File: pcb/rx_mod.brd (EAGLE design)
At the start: 42 x 28.7 mm, 25 parts, among them U1 ATMEGA328

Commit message: diversity ready version - TESTED
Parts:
- removed 3157: TS5A3157, pimoroni:SOT23-6
- removed ICSP1: 3x2 M, SmartPrj:2X03
- removed OLED: (no value), pinhead:1X04
- removed R_LED: 330, rcl:R0603
- removed R_PD_SWITCH: 10K, rcl:R0805
- removed STATUS: (no value), led:SML0603
- added C3: (no value), adafruit:C0603
- added JP3: (no value), SparkFun-Connectors:1X07
- added JP4: (no value), SparkFun-Connectors:1X04
- added LED_1, LED_2: (no value), led:SML0603
- added R_LED1, R_LED2: 330, rcl:R0603
- added R_RSSI1: 100K, SparkFun:0603-RES
- added U2: (no value), ts5a3359:VFSOP-8
- moved JP2 35.7 mm to (2.58, 8.29), turned to 270 degrees
- moved C_DTR 15.2 mm to (5.35, 14.9), flipped to the bottom
- moved R_PU_RST 15.0 mm to (5.35, 11.2), flipped to the bottom, turned to 270 degrees
- moved R_RSSI 5.95 mm to (27.4, 17.8), turned to 90 degrees
- moved R_CLK 4.89 mm to (36.8, 20.3), turned to 90 degrees
- moved R_VIDEO 4.26 mm to (13.7, 5.74)
- moved R_SYNC 3.56 mm to (16.9, 5.73)
- moved R_SPIDATA 3.28 mm to (33.8, 20.2), turned to 90 degrees
- moved R_VIDOUT 3.11 mm to (20.2, 6.07), turned to 90 degrees
- moved R_SPI_SEL 2.45 mm to (30.1, 20.3), turned to 90 degrees
- moved RECEIVER_A 2.30 mm to (7.07, 25.1)
- moved C2 2.13 mm to (25.3, 6.35)
- moved C1 1.76 mm to (33.3, 6.39)
- moved C_AREF 1.72 mm to (27.5, 14.1)
- moved XTAL1 1.44 mm to (11.2, 12.9)
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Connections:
- net SPI_SEL renamed SPI_SEL_A
- removed net LED_PIN: STATUS.A, U1.22
- new net N$11: LED_2.C, R_LED2.1
- new net RSSI_B: JP3.5, R_RSSI1.2, U1.24
- new net RXVIDOUT2: JP3.4, U2.1
- new net SPI_SEL_B: JP3.2, U1.12
- new net SW_CTRL2: LED_2.A, U1.10, U2.5
- net 5V: now also C3.1, JP3.7, U2.8; no longer 3157.5, ICSP1.2, OLED.4
- net GND: now also C3.2, JP3.6, R_LED1.2, R_LED2.2, R_RSSI1.1, U2.4; no longer 3157.2, ICSP1.6, OLED.3, R_LED.2, R_PD_SWITCH.1
- net MISO: now also JP4.3; no longer ICSP1.1
- net MOSI: now also JP4.2; no longer ICSP1.4
- net N$3: now also LED_1.C, R_LED1.1; no longer R_LED.1, STATUS.C
- net N$6: now also U2.7; no longer RECEIVER_A.VIDEO
- net OSD_VOUT: now also U2.3; no longer 3157.1
- net RESET: now also JP4.1; no longer ICSP1.5
- net RXVIDOUT: now also RECEIVER_A.VIDEO, U2.2; no longer 3157.3, C2.C, R_VIDOUT.2
- net SCK: now also JP4.4; no longer ICSP1.3
- net SCL: no longer OLED.2
- net SDA: no longer OLED.1
- net SPI_CLK: now also JP3.3
- net SPI_DATA: now also JP3.1
- net SW_CTRL: now also LED_1.A, U2.6; no longer 3157.6, R_PD_SWITCH.2
- net VIDOUT: now also C2.C, R_VIDOUT.2; no longer 3157.4
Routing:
- net GND: track 191.1 -> 117.2 mm, vias 4 -> 5
- net 5V: track 140.6 -> 82.7 mm, vias 3 -> 2
- net CH1: track 82.0 -> 45.6 mm, vias 10 -> 2
- net SW_CTRL2: track 0.00 -> 35.9 mm, vias 0 -> 2
- net RXVIDOUT2: track 0.00 -> 33.7 mm, vias 0 -> 1
- net LED_PIN: track 33.6 -> 0.00 mm, vias 4 -> 0
- net SPI_CLK: track 3.74 -> 33.5 mm
- net RXVIDOUT: track 11.7 -> 32.4 mm, vias 0 -> 1
- net SPI_SEL_B: track 0.00 -> 19.0 mm, vias 0 -> 3
- net SW_CTRL: track 20.8 -> 38.9 mm, vias 3 -> 2
- net MOSI: track 44.9 -> 27.8 mm, vias 6 -> 0
- net RSSI_B: track 0.00 -> 15.3 mm, vias 0 -> 1
- net SCK: track 36.8 -> 25.9 mm
- net SCL: track 10.8 -> 0.00 mm, vias 1 -> 0
- net N$6: track 20.6 -> 29.3 mm, vias 3 -> 2
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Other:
- board size 42 x 28.7 mm -> 42 x 28.8 mm
- board text added: "A"
- board text added: "B"
- board text added: "MISO"
- board text added: "MOSI"
- board text added: "OSD"
- board text added: "RST"
- board text added: "RX_VCC"
- board text added: "SCK"
- board text added: "SPI_CLK"
- board text added: "SPI_DATA"
- board text added: "SPI_SEL"
- board text added: "vidout"

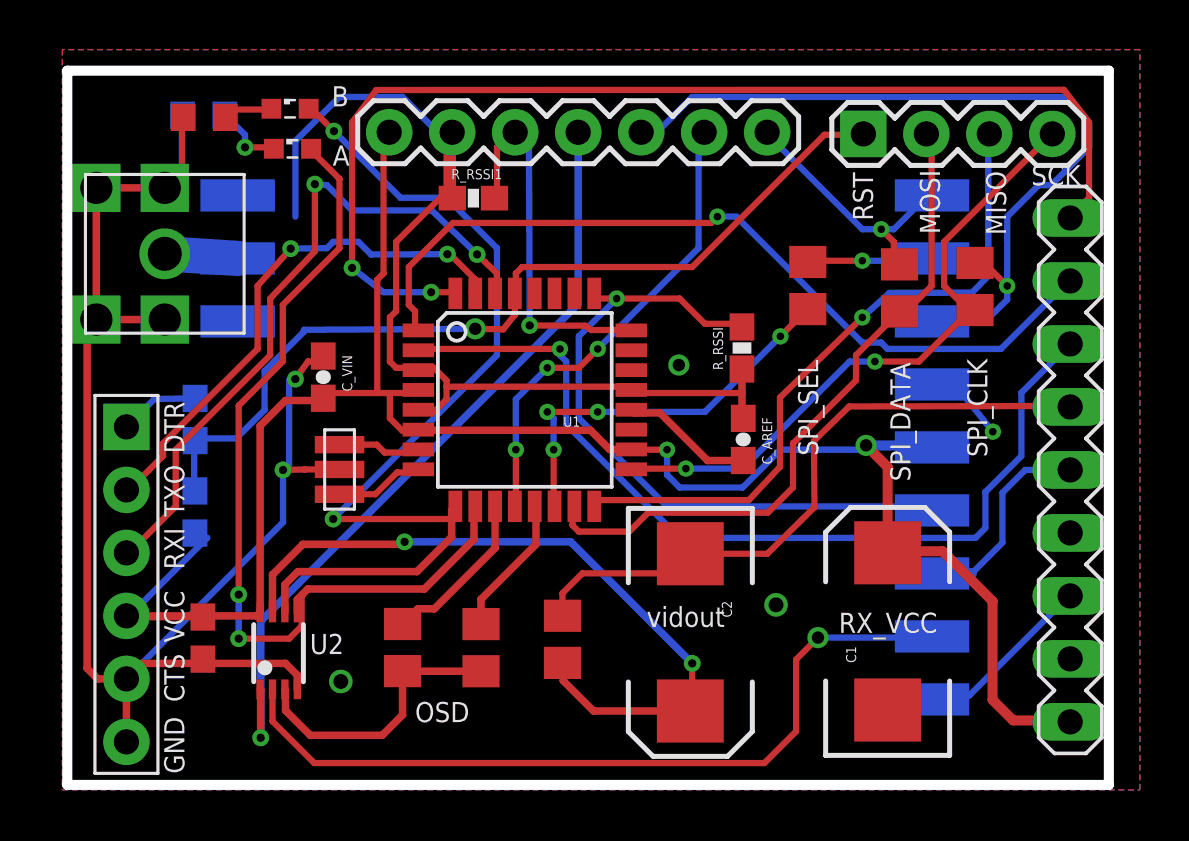
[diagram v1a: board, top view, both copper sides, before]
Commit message: new SMA connetor
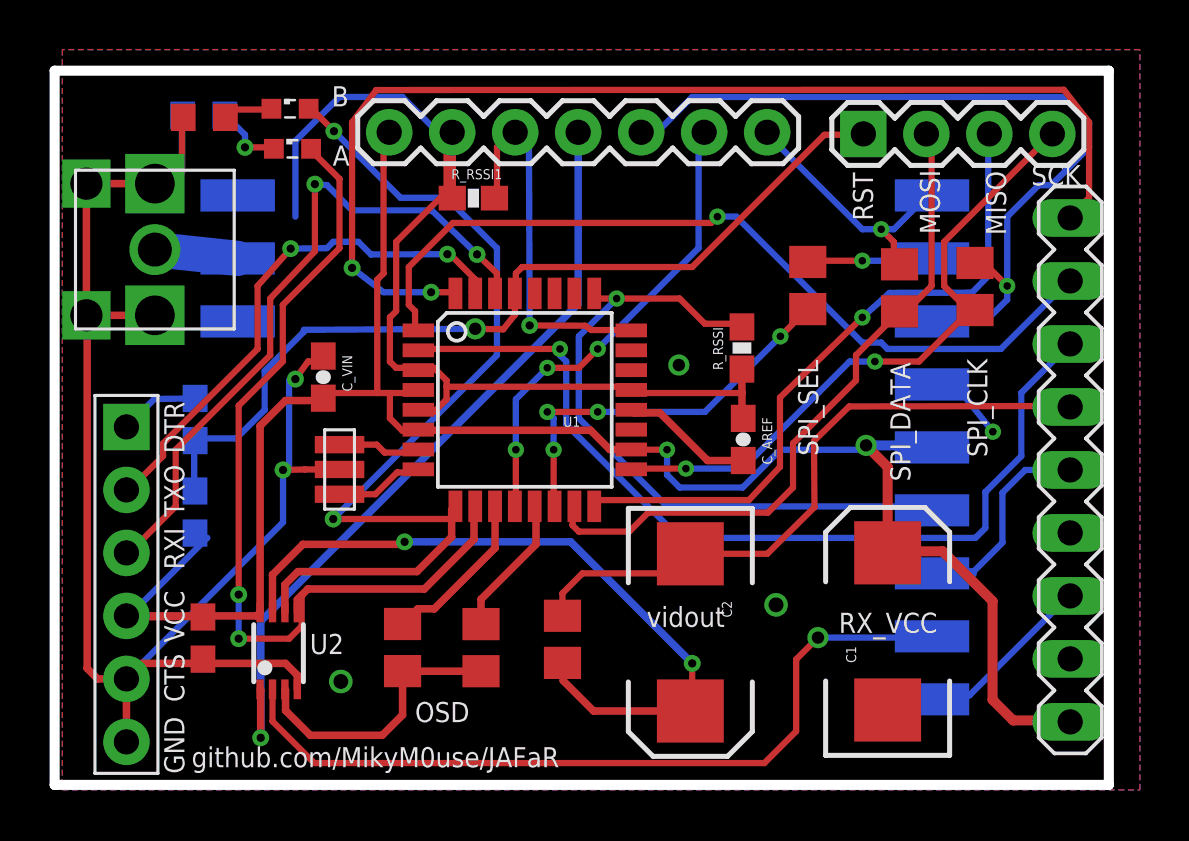
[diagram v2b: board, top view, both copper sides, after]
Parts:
- C1, C2: value (none) -> 470uf
- C3: value (none) -> 0.1uf
- moved U$1 0.43 mm to (3.71, 21.8)
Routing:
- net GND: track 117.2 -> 118.3 mm
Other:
- board size 42 x 28.8 mm -> 42.5 x 28.8 mm
- board text added: "github.com/MikyM0use/JAFaR"
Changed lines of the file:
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@@
 <?xml version="1.0" encoding="utf-8"?>
 <!DOCTYPE eagle SYSTEM "eagle.dtd">
-<eagle version="7.4.0">
+<eagle version="7.5.0">
 <drawing>
 <settings>
@@
 <board>
 <plain>
-<wire x1="0.2" y1="0.2" x2="0.2" y2="29" width="0.4064" layer="20"/>
-<wire x1="0.2" y1="29" x2="42.2" y2="29" width="0.4064" layer="20"/>
+<wire x1="-0.31" y1="0.2" x2="-0.31" y2="29" width="0.4064" layer="20"/>
+<wire x1="-0.31" y1="29" x2="42.2" y2="29" width="0.4064" layer="20"/>
 <wire x1="42.2" y1="29" x2="42.2" y2="0.2" width="0.4064" layer="20"/>
-<wire x1="42.2" y1="0.2" x2="0.2" y2="0.2" width="0.4064" layer="20"/>
+<wire x1="42.2" y1="0.2" x2="-0.31" y2="0.2" width="0.4064" layer="20"/>
 <text x="30.48" y="13.47" size="0.8128" layer="25" rot="R90">SPI_SEL</text>
 <text x="34.2" y="12.44" size="0.8128" layer="25" font="vector" rot="R90">SPI_DATA</text>
@@
 <text x="23.56" y="6.57" size="0.8128" layer="25" font="vector" ratio="9">vidout</text>
 <text x="31.31" y="6.33" size="0.8128" layer="25" font="vector" ratio="9">RX_VCC</text>
+<text x="5.21" y="0.91" size="0.8128" layer="25" font="vector">github.com/MikyM0use/JAFaR</text>
 </plain>
 <attributes>
@@
 </element>
 <element name="XTAL1" library="CSTCE16M0V53-R0" package="CSTCE16M0V53-R0" value="CSTCE16M0V53-R0" x="11.1798" y="12.9198" smashed="yes" rot="R270"/>
-<element name="U$1" library="#fpv" package="SMA_CONNECTOR" value="SMA_ANTENNA" x="4.1146" y="21.6352" rot="R90"/>
-<element name="C1" library="SparkFun-Passives" package="EIA7343" value="" x="33.28" y="6.39" rot="R90"/>
-<element name="C2" library="SparkFun-Passives" package="EIA7343" value="" x="25.3238" y="6.35" rot="R270"/>
+<element name="U$1" library="#fpv" package="SMA_CONNECTOR" value="SMA_ANTENNA" x="3.7146" y="21.8052" rot="R90"/>
+<element name="C1" library="SparkFun-Passives" package="EIA7343" value="470uf" x="33.28" y="6.39" rot="R90"/>
+<element name="C2" library="SparkFun-Passives" package="EIA7343" value="470uf" x="25.3238" y="6.35" rot="R270"/>
 <element name="R_VIDOUT" library="rcl" package="R0805" value="10" x="20.1676" y="6.0706" smashed="yes" rot="R90">
 <attribute name="VALUE" x="20.8562" y="9.0292" size="0.8128" layer="27" font="vector" rot="R180"/>
@@
 <attribute name="VALUE" x="8.28" y="23.85" size="1.27" layer="27"/>
 </element>
-<element name="C3" library="adafruit" package="C0603" value="" x="5.67" y="6.12" smashed="yes" rot="R270">
+<element name="C3" library="adafruit" package="C0603" value="0.1uf" x="5.67" y="6.12" smashed="yes" rot="R270">
 <attribute name="VALUE" x="3.638" y="7.009" size="1.27" layer="27" rot="R270"/>
 </element>
@@
 <wire x1="1.425" y1="4.475" x2="1" y2="4.9" width="0.3048" layer="1"/>
 <wire x1="1" y1="4.9" x2="1" y2="18.5936" width="0.3048" layer="1"/>
-<wire x1="1" y1="18.5936" x2="1.3716" y2="18.9652" width="0.3048" layer="1"/>
-<wire x1="1.3716" y1="18.9652" x2="4.1316" y2="18.9652" width="0.3048" layer="1"/>
-<wire x1="1.3716" y1="24.2752" x2="1.3716" y2="18.9652" width="0.3048" layer="1"/>
-<wire x1="1.3716" y1="24.2752" x2="4.1316" y2="24.2752" width="0.3048" layer="1"/>
+<wire x1="1" y1="18.5936" x2="0.9716" y2="19.1352" width="0.3048" layer="1"/>
+<wire x1="0.9716" y1="19.1352" x2="3.7316" y2="19.1352" width="0.3048" layer="1"/>
+<wire x1="0.9716" y1="24.4452" x2="0.9716" y2="19.1352" width="0.3048" layer="1"/>
+<wire x1="0.9716" y1="24.4452" x2="3.7316" y2="24.4452" width="0.3048" layer="1"/>
 <wire x1="9.475" y1="4.055" x2="9.475" y2="4.625" width="0.3048" layer="1"/>
 <wire x1="9.475" y1="4.625" x2="9" y2="5.1" width="0.3048" layer="1"/>
@@
 <wire x1="4.318" y1="24.384" x2="4.826" y2="24.892" width="0.254" layer="16"/>
 <wire x1="4.826" y1="27.178" x2="4.85" y2="27.2" width="0.254" layer="16"/>
-<wire x1="4.318" y1="24.384" x2="4.1316" y2="24.2752" width="0.254" layer="16"/>
+<wire x1="4.318" y1="24.384" x2="3.7316" y2="24.4452" width="0.254" layer="16"/>
 <wire x1="4.826" y1="24.892" x2="4.826" y2="26.924" width="0.254" layer="1"/>
 <wire x1="4.318" y1="24.384" x2="4.826" y2="24.892" width="0.254" layer="1"/>
 <wire x1="4.826" y1="26.924" x2="4.8746" y2="27.1168" width="0.254" layer="1"/>
-<wire x1="4.318" y1="24.384" x2="4.1316" y2="24.2752" width="0.254" layer="1"/>
+<wire x1="4.318" y1="24.384" x2="3.7316" y2="24.4452" width="0.254" layer="1"/>
 <wire x1="9.906" y1="17.272" x2="10.414" y2="17.272" width="0.254" layer="1"/>
 <wire x1="9.398" y1="16.564" x2="9.906" y2="17.272" width="0.254" layer="1"/>
@@
 <wire x1="9.398" y1="16.564" x2="9.144" y2="16.51" width="0.254" layer="16"/>
 <wire x1="9.144" y1="12.954" x2="8.9" y2="12.9" width="0.254" layer="16"/>
-<wire x1="4.826" y1="24.892" x2="4.1316" y2="24.2752" width="0.254" layer="16"/>
+<wire x1="4.826" y1="24.892" x2="3.7316" y2="24.4452" width="0.254" layer="16"/>
 <wire x1="14.986" y1="26.67" x2="15.494" y2="26.67" width="0.254" layer="16"/>
 <wire x1="13.716" y1="27.94" x2="14.986" y2="26.67" width="0.254" layer="16"/>
@@
 <contactref element="U$1" pad="ANT"/>
 <contactref element="RECEIVER_A" pad="ANT"/>
-<wire x1="7.07" y1="21.43" x2="4.1316" y2="21.6152" width="1.4224" layer="16"/>
+<wire x1="7.07" y1="21.43" x2="3.7316" y2="21.7852" width="1.4224" layer="16"/>
 </signal>
 <signal name="RSSI_B">
